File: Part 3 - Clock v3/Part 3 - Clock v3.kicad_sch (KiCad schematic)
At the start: 12 parts, among them J1 BUS 1, J2 RST/CLK TP, J3 AUX PWR, SW1 RESET, U1 74AHC14, U2 74AHC174

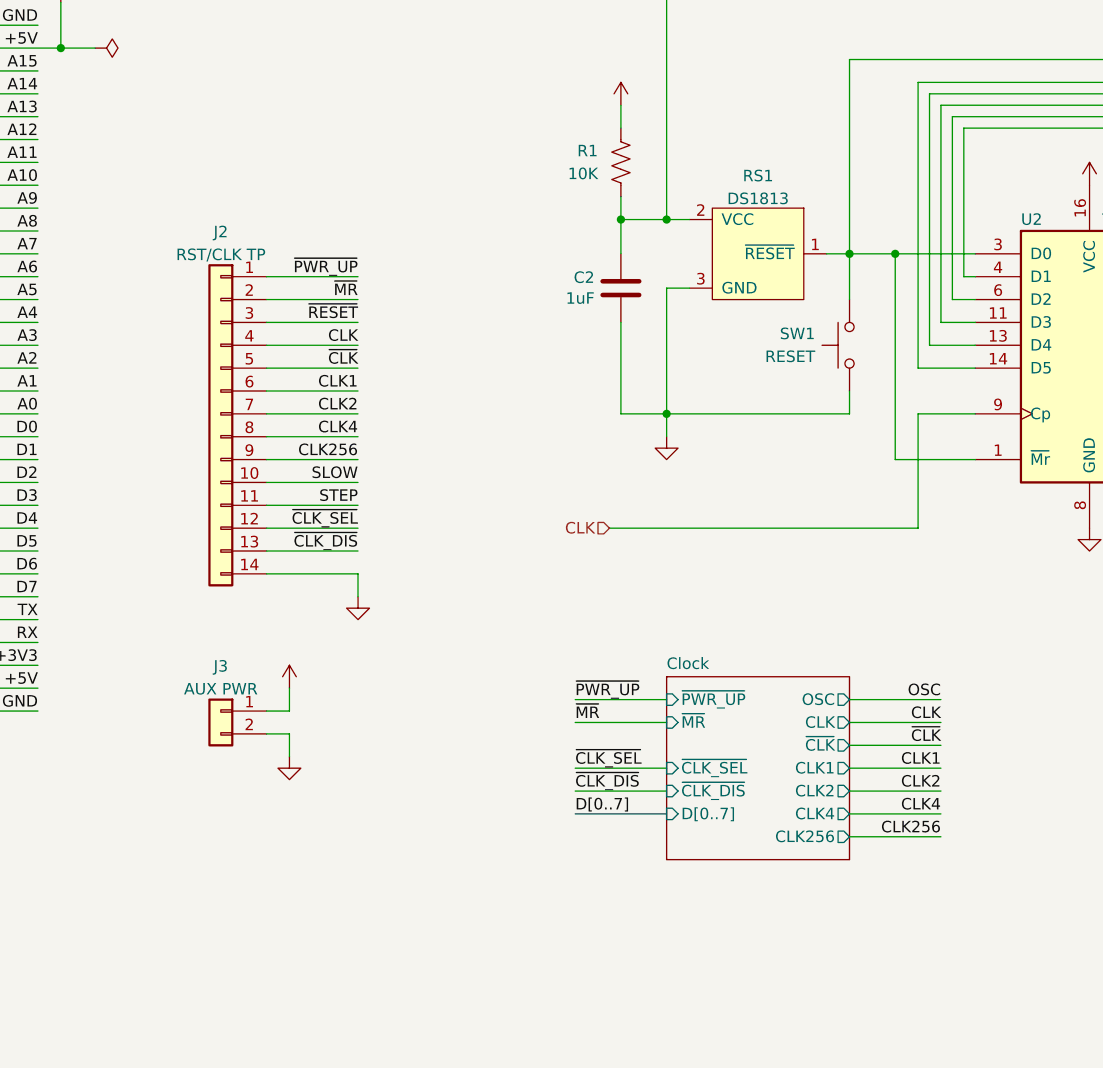
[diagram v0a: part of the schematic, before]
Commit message: Attempted to reduce chip count
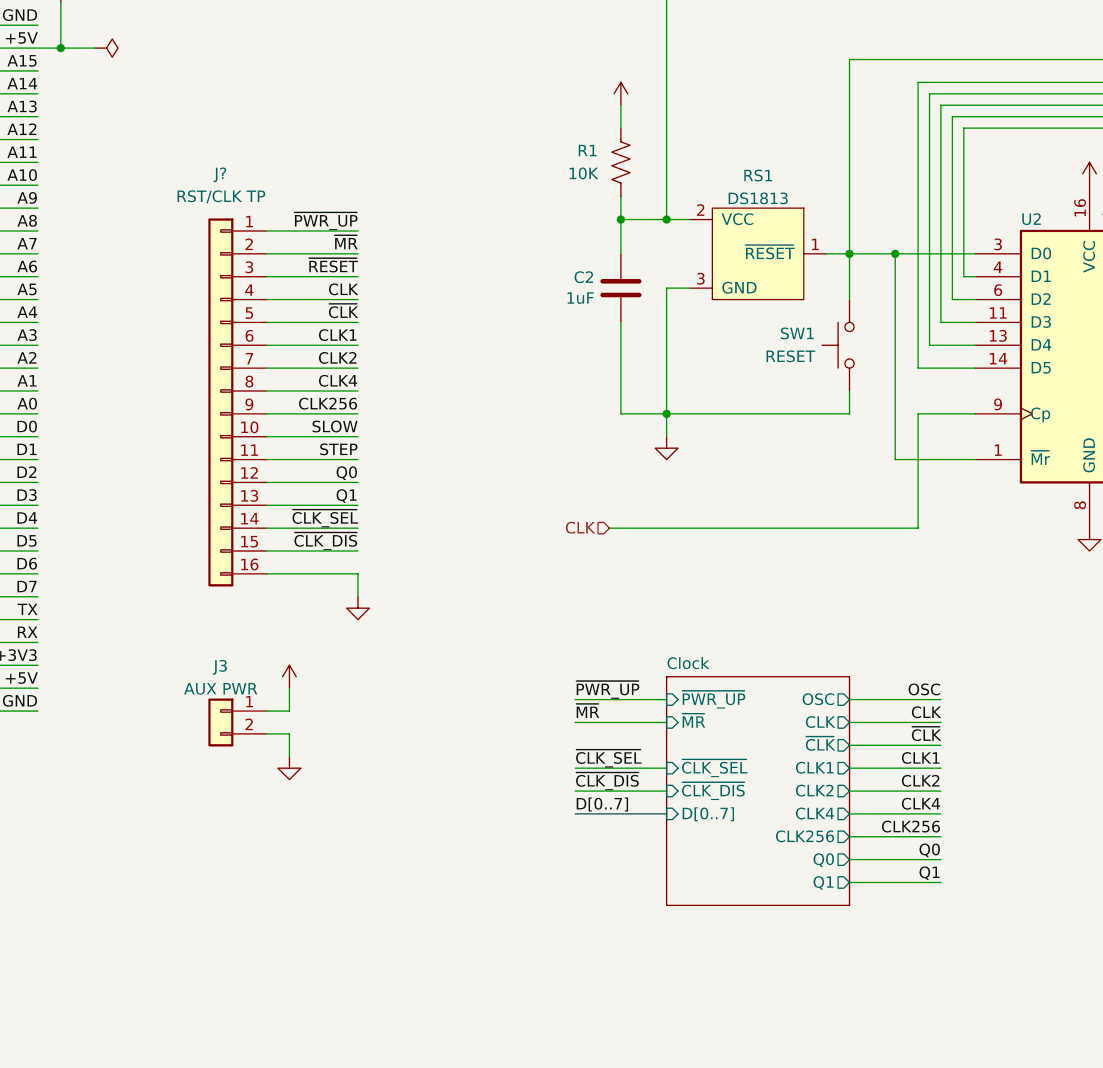
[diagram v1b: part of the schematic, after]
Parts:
- removed J2: RST/CLK TP, Connector_PinHeader_2.54mm:PinHeader_1x14_P2.54mm_Horizontal, symbol Connector_Generic:Conn_01x14
- added J?: RST/CLK TP, symbol Connector_Generic:Conn_01x16
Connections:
- net CLK: now also J?.4 (Pin_4)
- net CLK1: now also J?.6 (Pin_6)
- net CLK2: now also J?.7 (Pin_7)
- net CLK256: now also J?.9 (Pin_9)
- net CLK4: now also J?.8 (Pin_8)
- net GND: now also J?.16 (Pin_16)
- net SLOW: now also J?.10 (Pin_10)
- net STEP: now also J?.11 (Pin_11)
- net ~{CLK_DIS}: now also J?.15 (Pin_15)
- net ~{CLK_SEL}: now also J?.14 (Pin_14)
- net ~{CLK}: now also J?.5 (Pin_5)
- net ~{MR}: now also J?.2 (Pin_2)
- net ~{PWR_UP}: now also J?.1 (Pin_1)
- net ~{RESET}: now also J?.3 (Pin_3)
- new net Q0: J?.12 (Pin_12)
- new net Q1: J?.13 (Pin_13)
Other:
- sheet Clock ports: added Q0, Q1; removed none

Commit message: Clock 3 and Keyboard
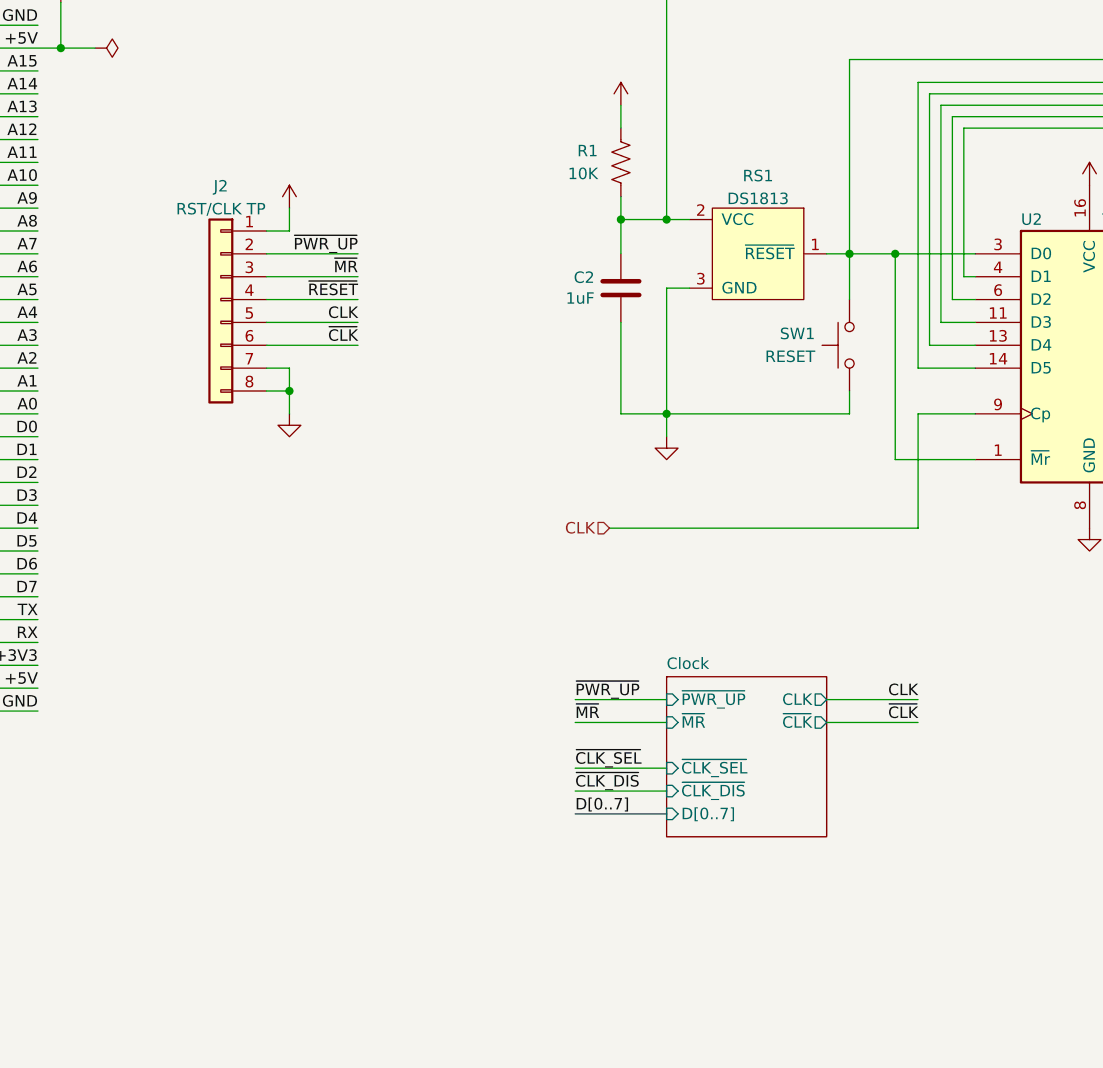
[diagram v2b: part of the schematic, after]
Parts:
- removed J3: AUX PWR, Connector_PinHeader_2.54mm:PinHeader_1x02_P2.54mm_Horizontal, symbol Connector_Generic:Conn_01x02
- removed J?: RST/CLK TP, symbol Connector_Generic:Conn_01x16
- added J2: RST/CLK TP, Connector_PinHeader_2.54mm:PinHeader_1x08_P2.54mm_Horizontal, symbol Connector_Generic:Conn_01x08
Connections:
- net +5V: now also J2.1 (Pin_1)
- net CLK: now also J2.5 (Pin_5)
- net GND: now also J2.7 (Pin_7), J2.8 (Pin_8)
- net ~{CLK}: now also J2.6 (Pin_6)
- net ~{MR}: now also J2.3 (Pin_3)
- net ~{PWR_UP}: now also J2.2 (Pin_2)
- net ~{RESET}: now also J2.4 (Pin_4)
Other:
- sheet Clock ports: added none; removed CLK1, CLK2, CLK256, CLK4, OSC, Q0, Q1

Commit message: Added Keyboard, and minor fixes
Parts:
- U1: value 74AHC14 -> 74AC14
- U2: value 74AHC174 -> 74AC174
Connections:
- net ~{IORD} renamed USER5
- net ~{IOWR} renamed USER6

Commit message: Long time backup
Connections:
- net CLK1 renamed USER7
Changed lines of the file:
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@@
     (effects (font (size 1.27 1.27)) (justify left bottom))
   )
-  (label "CLK1" (at 40.64 115.57 0)
+  (label "USER7" (at 40.64 115.57 0)
     (effects (font (size 1.27 1.27)) (justify left bottom))
   )
